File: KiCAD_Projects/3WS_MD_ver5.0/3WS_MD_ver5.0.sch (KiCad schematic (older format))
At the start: 149 parts, among them P1 CONN_01X02, P10 CONN_01X04, P11 TST, P12 CONN_02X08, P13 CONN_01X06, P14 CONN_01X02, P15 CONN_01X02, P16 CONN_01X04, P17 CONN_01X04, P2 CONN_01X02, P20 CONN_01X03, P3 CONN_01X04, P4 CONN_02X06, P5 TST, P6 CONN_01X04, P7 CONN_01X02, P8 CONN_01X04, P9 TST, Q1 MOSFET_N, Q2 MOSFET_N, Q3 MOSFET_N, Q4 MOSFET_N, Q5 MOSFET_N, Q6 MOSFET_N, Q7 MOSFET_N, Q8 MOSFET_N, SW1 SW_PUSH, SW2 SW_PUSH, SW3 SW_PUSH, U1 STM32F103_48, U10 NCP1117ST33T3G, U11 TBD62083A, U2 SI8234, U3 SI8234, U4 LM7812, U5 SI8234, U6 SI8234, U7 7805, U8 MAX3051, U9 SW_ROTARY_16, X2 CRYSTAL

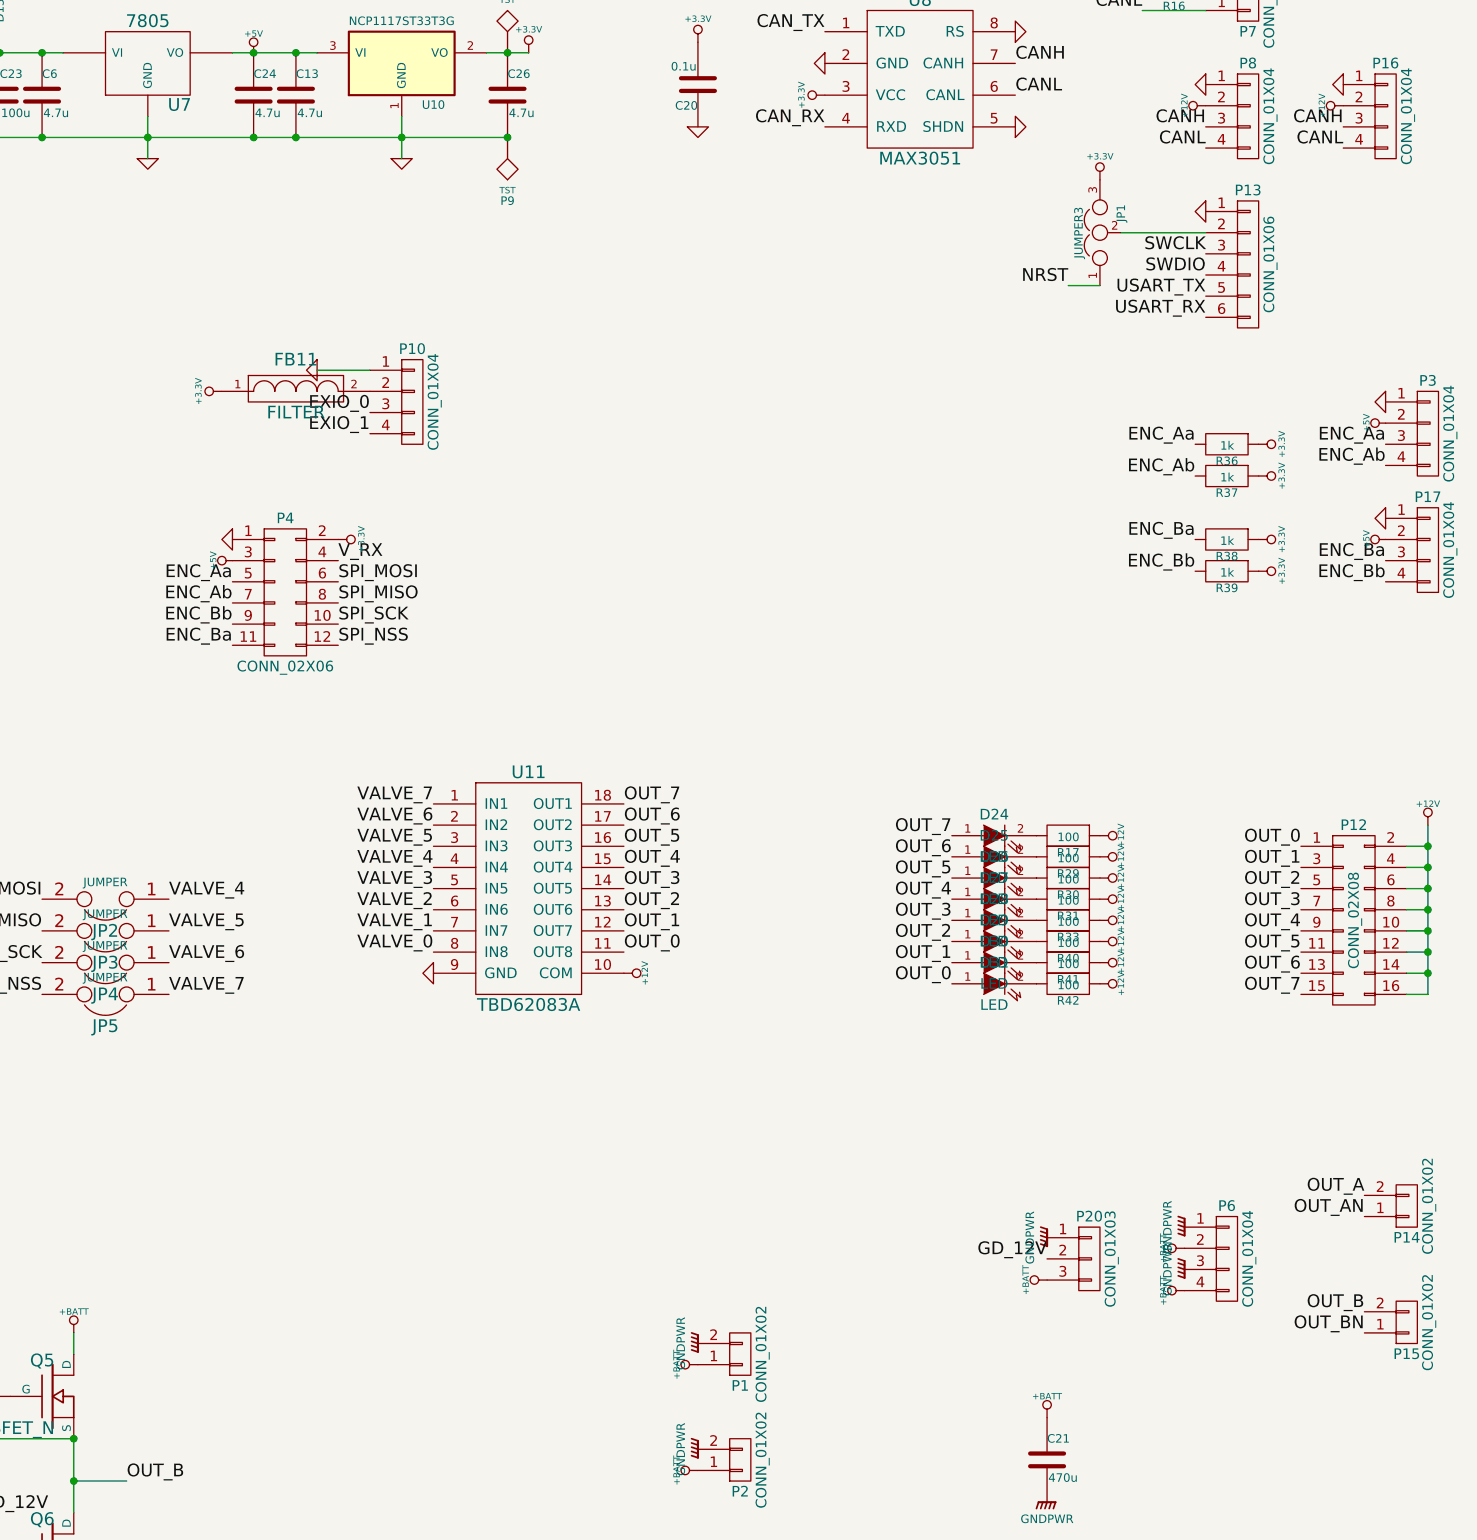
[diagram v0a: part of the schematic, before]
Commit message: ver5.0と5.0Exの設計終わり｡CAN node ver1.2の設計終わり｡BLMD基板設計開始｡ISO_DCDCver1.1設計開始｡
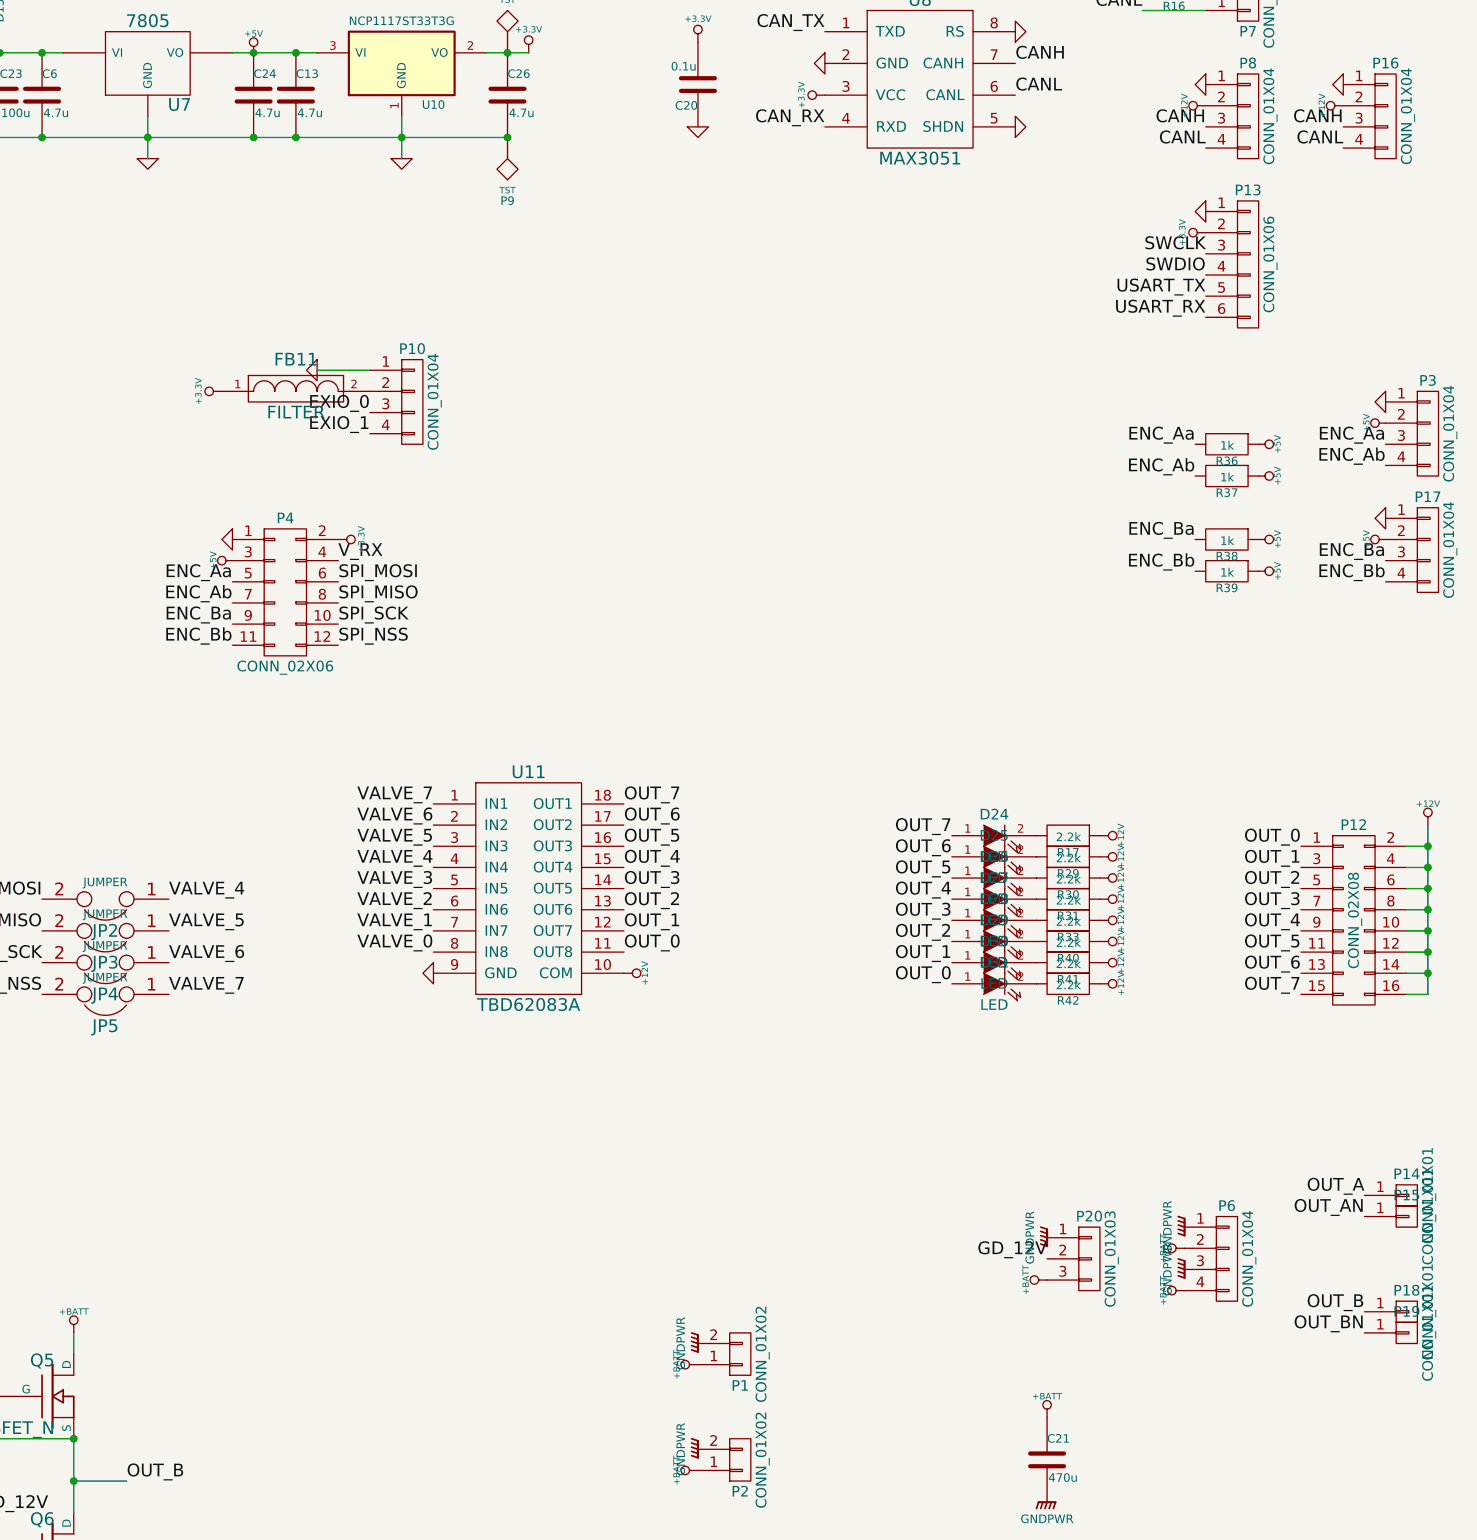
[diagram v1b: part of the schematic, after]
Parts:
- removed JP1: JUMPER3, Connect:GS3, symbol JUMPER3
- removed P14, P15: CONN_01X02, RP_KiCAD_Connector:DEANS_T_F, symbol CONN_01X02
- added P14, P15, P18, P19: CONN_01X01, RP_KiCAD_Connector:KRB-300, symbol CONN_01X01
- R17, R29, R30, R31, R33, R40, R41, R42: value 100 -> 2.2k
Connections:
- net +3.3V: now also P13.2 (P2); no longer R36.1, R37.1, R38.1, R39.1
- net +5V: now also R36.1, R37.1, R38.1, R39.1
- net ENC_Ba: now also P4.9 (P9); no longer P4.11 (P11)
- net ENC_Bb: now also P4.11 (P11); no longer P4.9 (P9)
- net OUT_A: now also P14.1 (P1)
- net OUT_AN: now also P15.1 (P1)
- net OUT_B: now also P18.1 (P1)
- net OUT_BN: now also P19.1 (P1)
